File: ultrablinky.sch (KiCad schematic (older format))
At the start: 125 parts, among them J1 DNP, J2 SJ1-3523N, J3 SJ1-3523N, J4 Barrel_Jack_5.5x2.5, J5 DNP, J6 DNP, J7 Terminal5, J8 SJ1-3523N, Q1 DMP6180SK3Q-13, Q2 DMP6180SK3Q-13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

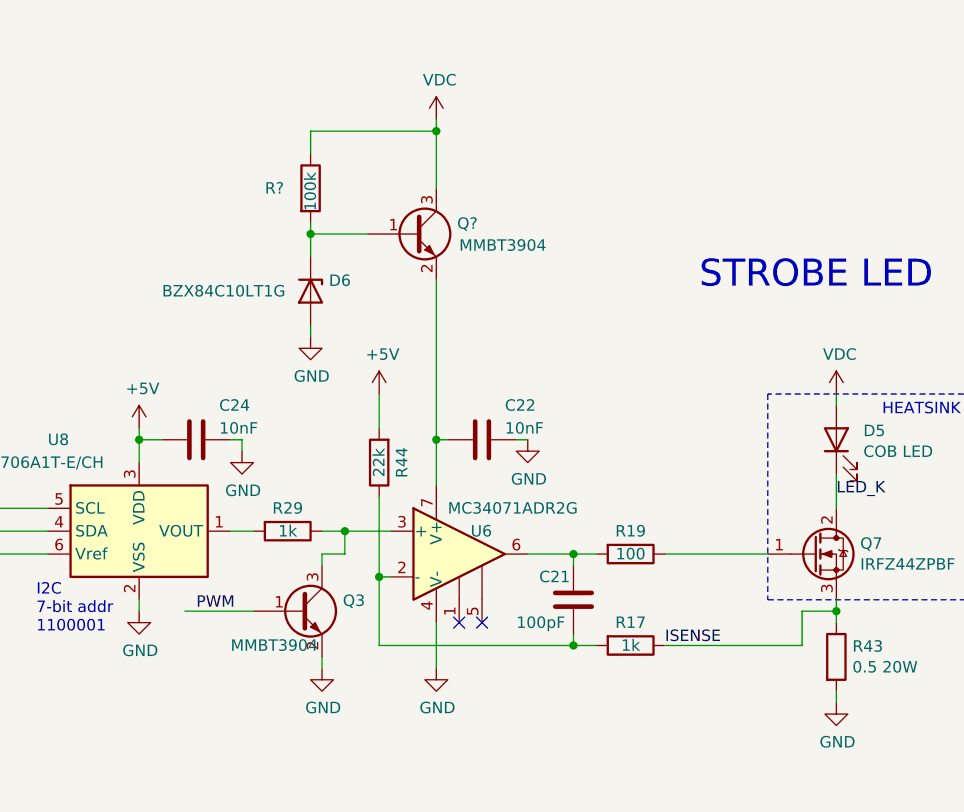
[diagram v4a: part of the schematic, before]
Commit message: Increase C22 to 22uF
C22 was changed to 22uF to provide better filter of the op amp power
supply
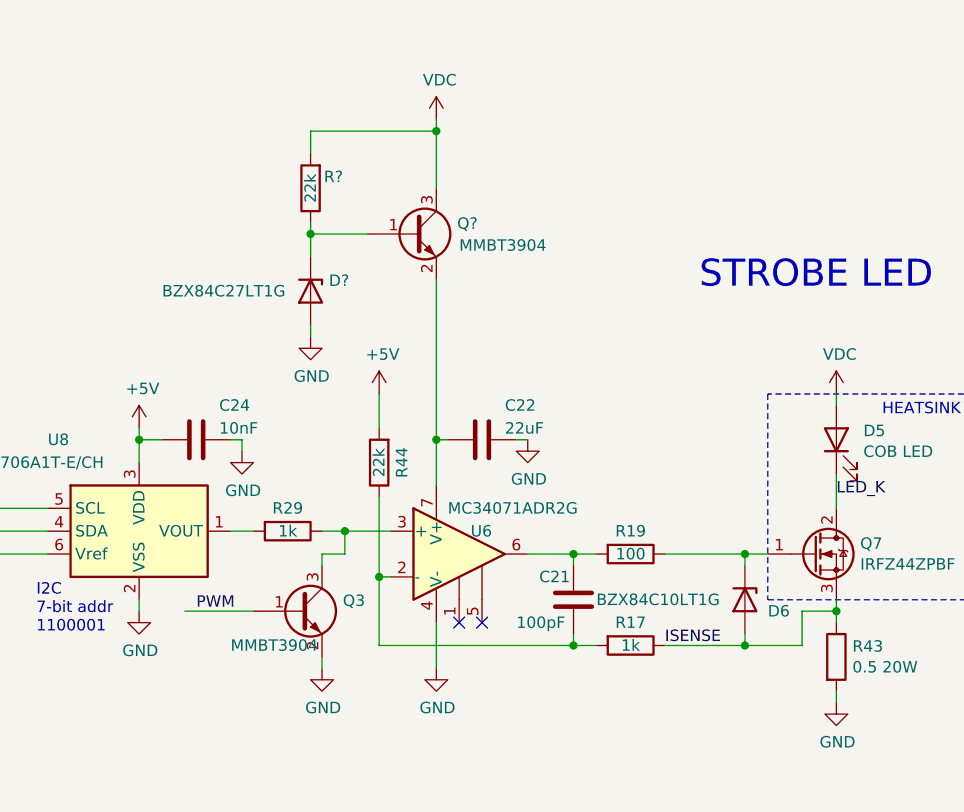
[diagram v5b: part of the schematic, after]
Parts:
- removed R?: 100k, Resistor_SMD:R_0805_2012Metric, symbol Device:R
- added D?: BZX84C27LT1G, Diode_SMD:D_SOT-23_ANK, symbol Diode:BZX84Cxx
- added R?: 22k, Resistor_SMD:R_0805_2012Metric, symbol Device:R
- C22: value 10nF -> 22uF; footprint Capacitor_SMD:C_0805_2012Metric -> Capacitor_SMD:C_1210_3225Metric; Source Mouser 80-C0805C103K1R -> Mouser 187-CL32A226MOJNNNE
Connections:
- wire segments 383 -> 387
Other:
- moved on the sheet: D6
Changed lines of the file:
@@
 P 3900 6250
 F 0 "C22" V 3750 6350 50  0000 L CNN
-F 1 "10nF" V 3850 6350 50  0000 L CNN
-F 2 "Capacitor_SMD:C_0805_2012Metric" H 3938 6100 50  0001 C CNN
+F 1 "22uF" V 3850 6350 50  0000 L CNN
+F 2 "Capacitor_SMD:C_1210_3225Metric" H 3938 6100 50  0001 C CNN
 F 3 "~" H 3900 6250 50  0001 C CNN
-F 4 "Mouser 80-C0805C103K1R" H 3900 6250 50  0001 C CNN "Source"
+F 4 "Mouser 187-CL32A226MOJNNNE" H 3900 6250 50  0001 C CNN "Source"
 	1    3900 6250
 	0    1    1    0
@@
 L Diode:BZX84Cxx D6
 U 1 1 60EC40DE
-P 3150 5600
-F 0 "D6" V 3104 5680 50  0000 L CNN
-F 1 "BZX84C10LT1G" V 3150 4950 50  0000 L CNN
-F 2 "Diode_SMD:D_SOT-23_ANK" H 3150 5425 50  0001 C CNN
-F 3 "https://diotec.com/tl_files/diotec/files/pdf/datasheets/bzx84c2v4.pdf" H 3150 5600 50  0001 C CNN
-F 4 "Mouser 863-BZX84C10LT1G" H 3150 5600 50  0001 C CNN "Source"
-	1    3150 5600
+P 5050 6950
+F 0 "D6" V 5100 7050 50  0000 L CNN
+F 1 "BZX84C10LT1G" V 5050 6300 50  0000 L CNN
+F 2 "Diode_SMD:D_SOT-23_ANK" H 5050 6775 50  0001 C CNN
+F 3 "https://diotec.com/tl_files/diotec/files/pdf/datasheets/bzx84c2v4.pdf" H 5050 6950 50  0001 C CNN
+F 4 "Mouser 863-BZX84C10LT1G" H 5050 6950 50  0001 C CNN "Source"
+	1    5050 6950
 	0    1    1    0
 $EndComp
@@
 	3700 5550 3700 6250
 Wire Wire Line
-	4700 7150 5300 7150
-Wire Wire Line
-	4700 6750 5150 6750
+	4700 7150 5050 7150
+Wire Wire Line
+	4700 6750 5050 6750
 $Comp
 L power:GND #PWR?
@@
 Wire Wire Line
 	3700 4850 3700 4900
+Wire Wire Line
+	3150 5300 3150 5350
+Connection ~ 3150 5350
+Wire Wire Line
+	3150 5000 3150 4900
+Wire Wire Line
+	3150 4900 3700 4900
+Connection ~ 3700 4900
+Wire Wire Line
+	3700 4900 3700 5150
+Wire Wire Line
+	1000 3350 2400 3350
+Wire Wire Line
+	1000 3450 2400 3450
+Wire Wire Line
+	5050 6800 5050 6750
+Connection ~ 5050 6750
+Wire Wire Line
+	5050 6750 5150 6750
+Wire Wire Line
+	5050 7100 5050 7150
+Connection ~ 5050 7150
+Wire Wire Line
+	5050 7150 5300 7150
+$Comp
+L Diode:BZX84Cxx D?
+U 1 1 612A00AB
+P 3150 5600
+F 0 "D?" V 3104 5680 50  0000 L CNN
+F 1 "BZX84C27LT1G " V 3150 4950 50  0000 L CNN
+F 2 "Diode_SMD:D_SOT-23_ANK" H 3150 5425 50  0001 C CNN
+F 3 "https://diotec.com/tl_files/diotec/files/pdf/datasheets/bzx84c2v4.pdf" H 3150 5600 50  0001 C CNN
+F 4 "Mouser 863-BZX84C27LT1G " H 3150 5600 50  0001 C CNN "Source"
+	1    3150 5600
+	0    1    1    0
+$EndComp
 $Comp
 L Device:R R?
-U 1 1 6117A498
+U 1 1 612C6BB1
 P 3150 5150
-F 0 "R?" H 2950 5150 50  0000 L CNN
-F 1 "100k" V 3150 5050 50  0000 L CNN
+F 0 "R?" H 3050 5100 50  0000 C CNN
+F 1 "22k" V 3150 5150 50  0000 C CNN
 F 2 "Resistor_SMD:R_0805_2012Metric" V 3080 5150 50  0001 C CNN
 F 3 "~" H 3150 5150 50  0001 C CNN
-F 4 "Mouser 603-RC0805JR-07100KL" H 3150 5150 50  0001 C CNN "Source"
+F 4 "Mouser 603-RC0805JR-0722KL" H 3150 5150 50  0001 C CNN "Source"
 	1    3150 5150
-	1    0    0    -1
-$EndComp
-Wire Wire Line
-	3150 5300 3150 5350
-Connection ~ 3150 5350
-Wire Wire Line
-	3150 5000 3150 4900
-Wire Wire Line
-	3150 4900 3700 4900
-Connection ~ 3700 4900
-Wire Wire Line
-	3700 4900 3700 5150
-Wire Wire Line
-	1000 3350 2400 3350
-Wire Wire Line
-	1000 3450 2400 3450
+	-1   0    0    1
+$EndComp
 $EndSCHEMATC
